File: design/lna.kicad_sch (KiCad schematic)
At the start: 19 parts, among them J5 SMA, U10 ADA4930-1

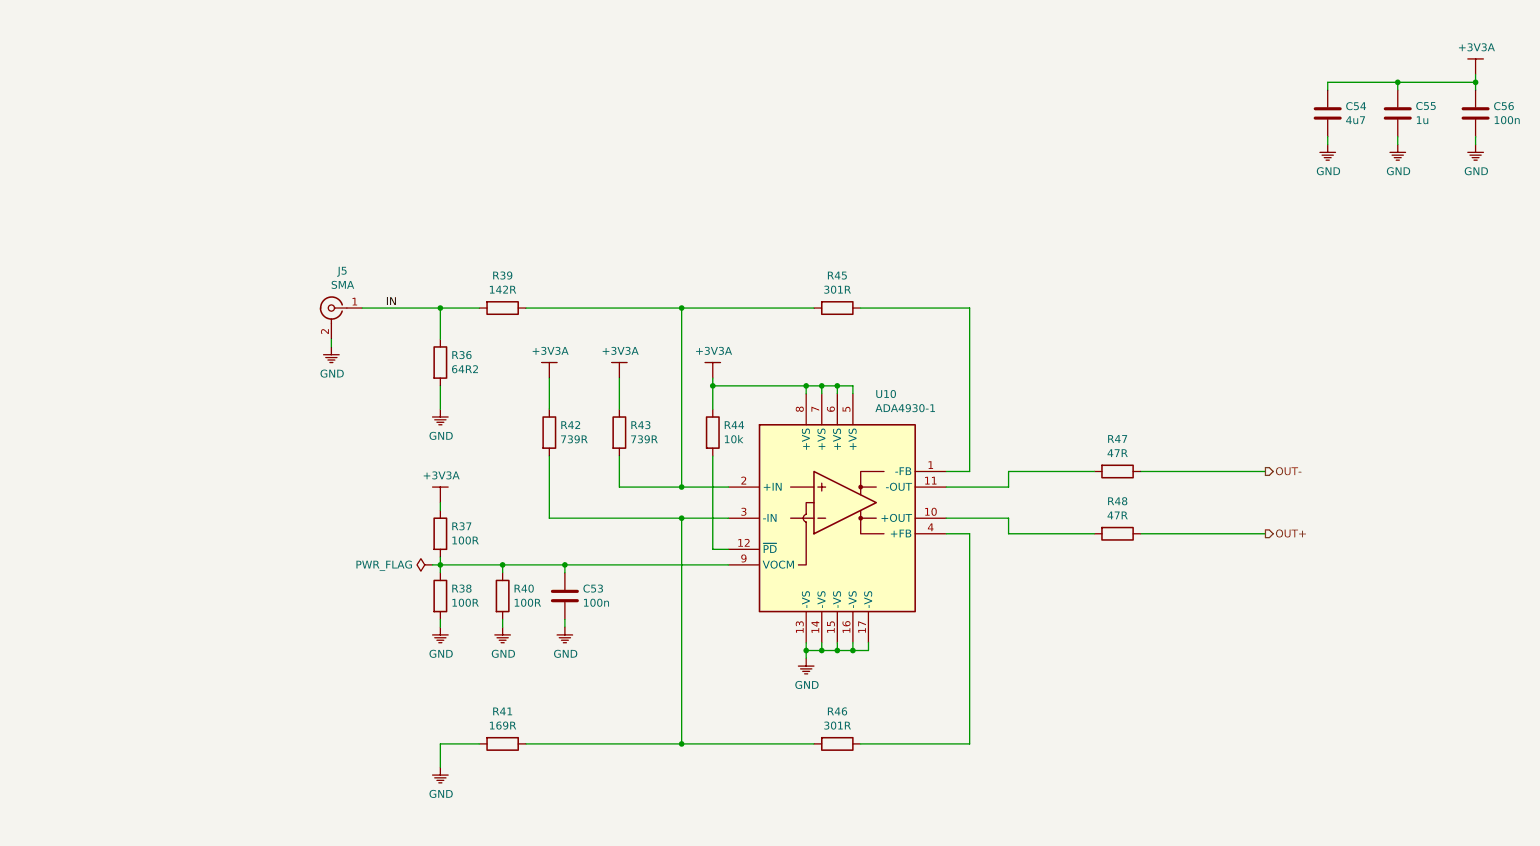
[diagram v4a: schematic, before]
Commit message: Added fiducials
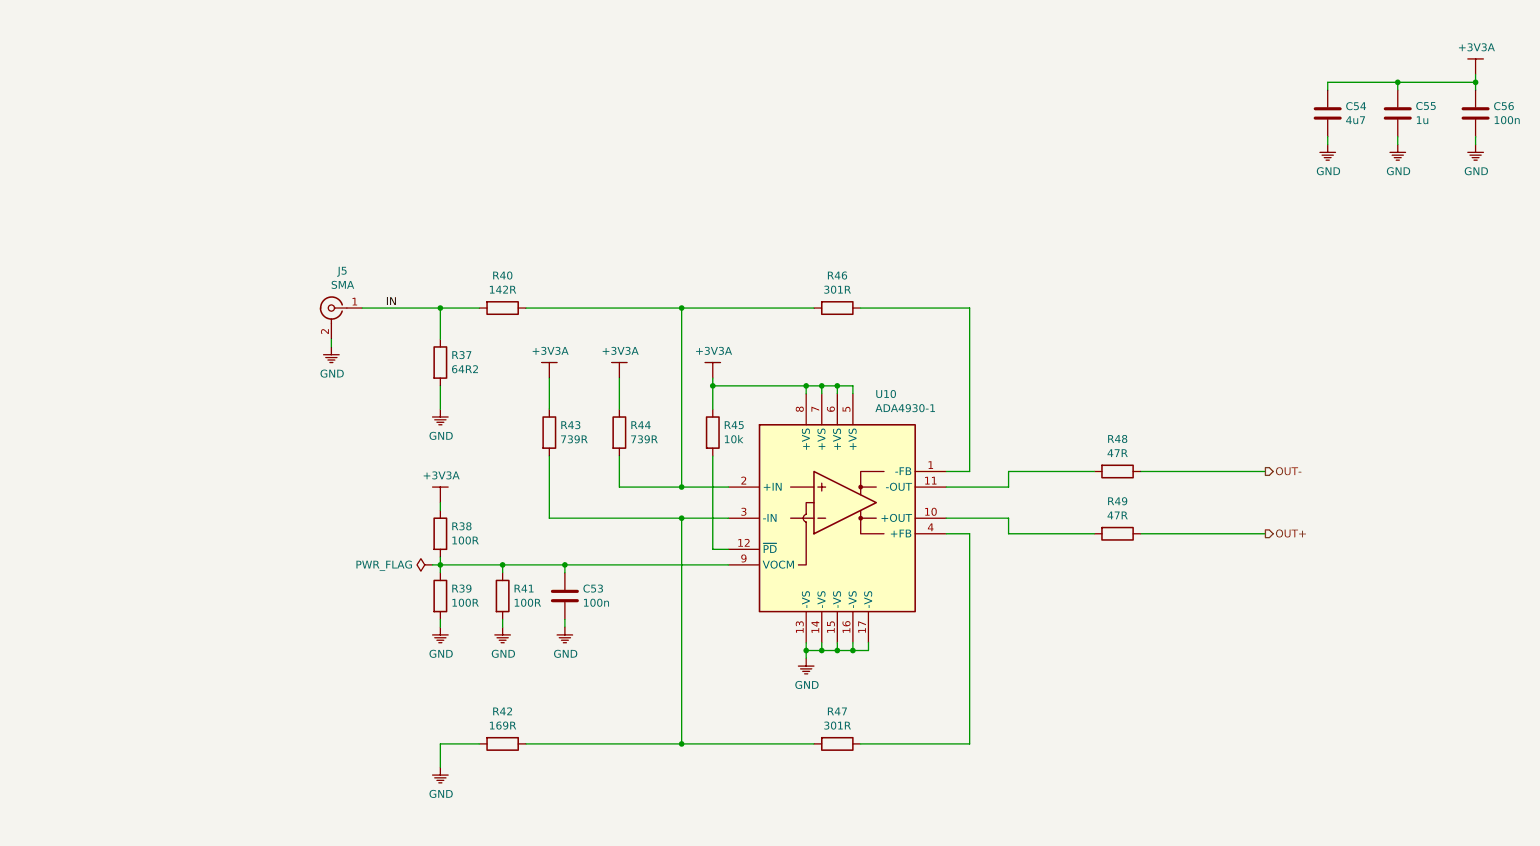
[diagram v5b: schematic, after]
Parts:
- renumbered R36 to R37, R37 to R38, R38 to R39, R39 to R40, R40 to R41, R41 to R42, R42 to R43, R43 to R44, R44 to R45, R45 to R46, R46 to R47, R47 to R48, R48 to R49
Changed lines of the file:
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@@
   )
   (symbol (lib_id "KLIB_Power:GND") (at 67.31 69.85 0) (unit 1)
-    (property "Reference" "#PWR0108" (id 0) (at 67.31 74.93 0)
+    (property "Reference" "#PWR0111" (id 0) (at 67.31 74.93 0)
       (effects (font (size 1.27 1.27)) hide)
     )
@@
   )
   (symbol (lib_id "KLIB_Power:GND") (at 85.09 80.01 0) (unit 1)
-    (property "Reference" "#PWR0109" (id 0) (at 85.09 85.09 0)
+    (property "Reference" "#PWR0112" (id 0) (at 85.09 85.09 0)
       (effects (font (size 1.27 1.27)) hide)
     )
@@
   )
   (symbol (lib_id "KLIB_Power:+3V3A") (at 85.09 95.25 0) (unit 1)
-    (property "Reference" "#PWR0110" (id 0) (at 85.09 102.87 0)
+    (property "Reference" "#PWR0113" (id 0) (at 85.09 102.87 0)
       (effects (font (size 1.27 1.27)) hide)
     )
@@
   )
   (symbol (lib_id "KLIB_Power:GND") (at 85.09 115.57 0) (unit 1)
-    (property "Reference" "#PWR0111" (id 0) (at 85.09 120.65 0)
+    (property "Reference" "#PWR0114" (id 0) (at 85.09 120.65 0)
       (effects (font (size 1.27 1.27)) hide)
     )
@@
   )
   (symbol (lib_id "KLIB_Power:GND") (at 85.09 138.43 0) (unit 1)
-    (property "Reference" "#PWR0112" (id 0) (at 85.09 143.51 0)
+    (property "Reference" "#PWR0115" (id 0) (at 85.09 143.51 0)
       (effects (font (size 1.27 1.27)) hide)
     )
@@
   )
   (symbol (lib_id "KLIB_Power:GND") (at 95.25 115.57 0) (unit 1)
-    (property "Reference" "#PWR0113" (id 0) (at 95.25 120.65 0)
+    (property "Reference" "#PWR0116" (id 0) (at 95.25 120.65 0)
       (effects (font (size 1.27 1.27)) hide)
     )
@@
   )
   (symbol (lib_id "KLIB_Power:+3V3A") (at 102.87 74.93 0) (unit 1)
-    (property "Reference" "#PWR0114" (id 0) (at 102.87 82.55 0)
+    (property "Reference" "#PWR0117" (id 0) (at 102.87 82.55 0)
       (effects (font (size 1.27 1.27)) hide)
     )
@@
   )
   (symbol (lib_id "KLIB_Power:GND") (at 105.41 115.57 0) (unit 1)
-    (property "Reference" "#PWR0115" (id 0) (at 105.41 120.65 0)
+    (property "Reference" "#PWR0118" (id 0) (at 105.41 120.65 0)
       (effects (font (size 1.27 1.27)) hide)
     )
@@
   )
   (symbol (lib_id "KLIB_Power:+3V3A") (at 114.3 74.93 0) (unit 1)
-    (property "Reference" "#PWR0116" (id 0) (at 114.3 82.55 0)
+    (property "Reference" "#PWR0119" (id 0) (at 114.3 82.55 0)
       (effects (font (size 1.27 1.27)) hide)
     )
@@
   )
   (symbol (lib_id "KLIB_Power:+3V3A") (at 129.54 74.93 0) (unit 1)
-    (property "Reference" "#PWR0117" (id 0) (at 129.54 82.55 0)
+    (property "Reference" "#PWR0120" (id 0) (at 129.54 82.55 0)
       (effects (font (size 1.27 1.27)) hide)
     )
@@
   )
   (symbol (lib_id "KLIB_Power:GND") (at 144.78 120.65 0) (unit 1)
-    (property "Reference" "#PWR0118" (id 0) (at 144.78 125.73 0)
+    (property "Reference" "#PWR0121" (id 0) (at 144.78 125.73 0)
       (effects (font (size 1.27 1.27)) hide)
     )
@@
   )
   (symbol (lib_id "KLIB_Power:GND") (at 229.87 36.83 0) (unit 1)
-    (property "Reference" "#PWR0119" (id 0) (at 229.87 41.91 0)
+    (property "Reference" "#PWR0122" (id 0) (at 229.87 41.91 0)
       (effects (font (size 1.27 1.27)) hide)
     )
@@
   )
   (symbol (lib_id "KLIB_Power:GND") (at 241.3 36.83 0) (unit 1)
-    (property "Reference" "#PWR0120" (id 0) (at 241.3 41.91 0)
+    (property "Reference" "#PWR0123" (id 0) (at 241.3 41.91 0)
       (effects (font (size 1.27 1.27)) hide)
     )
@@
   )
   (symbol (lib_id "KLIB_Power:+3V3A") (at 254 25.4 0) (unit 1)
-    (property "Reference" "#PWR0121" (id 0) (at 254 33.02 0)
+    (property "Reference" "#PWR0124" (id 0) (at 254 33.02 0)
       (effects (font (size 1.27 1.27)) hide)
     )
@@
   )
   (symbol (lib_id "KLIB_Power:GND") (at 254 36.83 0) (unit 1)
-    (property "Reference" "#PWR0122" (id 0) (at 254 41.91 0)
+    (property "Reference" "#PWR0125" (id 0) (at 254 41.91 0)
       (effects (font (size 1.27 1.27)) hide)
     )
@@
   )
   (symbol (lib_id "Device:R") (at 85.09 72.39 0) (unit 1)
-    (property "Reference" "R36" (id 0) (at 86.868 71.2216 0)
+    (property "Reference" "R37" (id 0) (at 86.868 71.2216 0)
       (effects (font (size 1.27 1.27)) (justify left))
     )
@@
   )
   (symbol (lib_id "Device:R") (at 85.09 100.33 0) (unit 1)
-    (property "Reference" "R37" (id 0) (at 86.868 99.1616 0)
+    (property "Reference" "R38" (id 0) (at 86.868 99.1616 0)
       (effects (font (size 1.27 1.27)) (justify left))
     )
@@
   )
   (symbol (lib_id "Device:R") (at 85.09 110.49 0) (unit 1)
-    (property "Reference" "R38" (id 0) (at 86.868 109.3216 0)
+    (property "Reference" "R39" (id 0) (at 86.868 109.3216 0)
       (effects (font (size 1.27 1.27)) (justify left))
     )
@@
   )
   (symbol (lib_id "Device:R") (at 95.25 63.5 270) (unit 1)
-    (property "Reference" "R39" (id 0) (at 95.25 58.2422 90))
+    (property "Reference" "R40" (id 0) (at 95.25 58.2422 90))
     (property "Value" "142R" (id 1) (at 95.25 60.5536 90))
     (property "Footprint" "Resistor_SMD:R_0603_1608Metric" (id 2) (at 95.25 61.722 90)
@@
   )
   (symbol (lib_id "Device:R") (at 95.25 110.49 0) (unit 1)
-    (property "Reference" "R40" (id 0) (at 97.028 109.3216 0)
+    (property "Reference" "R41" (id 0) (at 97.028 109.3216 0)
       (effects (font (size 1.27 1.27)) (justify left))
     )
@@
   )
   (symbol (lib_id "Device:R") (at 95.25 134.62 270) (unit 1)
-    (property "Reference" "R41" (id 0) (at 95.25 129.3622 90))
+    (property "Reference" "R42" (id 0) (at 95.25 129.3622 90))
     (property "Value" "169R" (id 1) (at 95.25 131.6736 90))
     (property "Footprint" "Resistor_SMD:R_0603_1608Metric" (id 2) (at 95.25 132.842 90)
@@
   )
   (symbol (lib_id "Device:R") (at 102.87 83.82 0) (unit 1)
-    (property "Reference" "R42" (id 0) (at 104.648 82.6516 0)
+    (property "Reference" "R43" (id 0) (at 104.648 82.6516 0)
       (effects (font (size 1.27 1.27)) (justify left))
     )
@@
   )
   (symbol (lib_id "Device:R") (at 114.3 83.82 0) (unit 1)
-    (property "Reference" "R43" (id 0) (at 116.078 82.6516 0)
+    (property "Reference" "R44" (id 0) (at 116.078 82.6516 0)
       (effects (font (size 1.27 1.27)) (justify left))
     )
@@
   )
   (symbol (lib_id "Device:R") (at 129.54 83.82 0) (unit 1)
-    (property "Reference" "R44" (id 0) (at 131.318 82.6516 0)
+    (property "Reference" "R45" (id 0) (at 131.318 82.6516 0)
       (effects (font (size 1.27 1.27)) (justify left))
     )
@@
   )
   (symbol (lib_id "Device:R") (at 149.86 63.5 270) (unit 1)
-    (property "Reference" "R45" (id 0) (at 149.86 58.2422 90))
+    (property "Reference" "R46" (id 0) (at 149.86 58.2422 90))
     (property "Value" "301R" (id 1) (at 149.86 60.5536 90))
     (property "Footprint" "Resistor_SMD:R_0603_1608Metric" (id 2) (at 149.86 61.722 90)
@@
   )
   (symbol (lib_id "Device:R") (at 149.86 134.62 270) (unit 1)
-    (property "Reference" "R46" (id 0) (at 149.86 129.3622 90))
+    (property "Reference" "R47" (id 0) (at 149.86 129.3622 90))
     (property "Value" "301R" (id 1) (at 149.86 131.6736 90))
     (property "Footprint" "Resistor_SMD:R_0603_1608Metric" (id 2) (at 149.86 132.842 90)
@@
   )
   (symbol (lib_id "Device:R") (at 195.58 90.17 270) (unit 1)
-    (property "Reference" "R47" (id 0) (at 195.58 84.9122 90))
+    (property "Reference" "R48" (id 0) (at 195.58 84.9122 90))
     (property "Value" "47R" (id 1) (at 195.58 87.2236 90))
     (property "Footprint" "Resistor_SMD:R_0402_1005Metric" (id 2) (at 195.58 88.392 90)
@@
   )
   (symbol (lib_id "Device:R") (at 195.58 100.33 270) (unit 1)
-    (property "Reference" "R48" (id 0) (at 195.58 95.0722 90))
+    (property "Reference" "R49" (id 0) (at 195.58 95.0722 90))
     (property "Value" "47R" (id 1) (at 195.58 97.3836 90))
     (property "Footprint" "Resistor_SMD:R_0402_1005Metric" (id 2) (at 195.58 98.552 90)

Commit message: Updated schematic
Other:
- note added: "LNA BYPASS"
- moved on the sheet: C53, C54, C55, C56, J5, R37, R38, R39, R40, R41, R42, R43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

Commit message: Updated LNA
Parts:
- R37: value 64R2 -> 56R2
- R38, R39, R41: value 100R -> 56R2
- R40: value 142R -> 301R
- R42: value 169R -> 301R
- R43, R44: value 739R -> 4k7
